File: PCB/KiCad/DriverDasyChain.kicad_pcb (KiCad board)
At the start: 4 copper layers, 70 x 70 mm, 50 parts, among them J1 Conn_01x03, J10 Conn_01x04, J12 Conn_01x04, J2 Conn_01x03, J3 Conn_01x03, J4 Conn_01x04, J5 Conn_01x03, J6 Conn_01x04, Q2 Q_NMOS_GDS, SW1 SW_DIP_x02, SW2 SW_SPDT, U1 AP2112K-3.3, U2 XIAO-ESP32-S3-DIP, U3 74AHCT1G125, U4 SN65HVD230

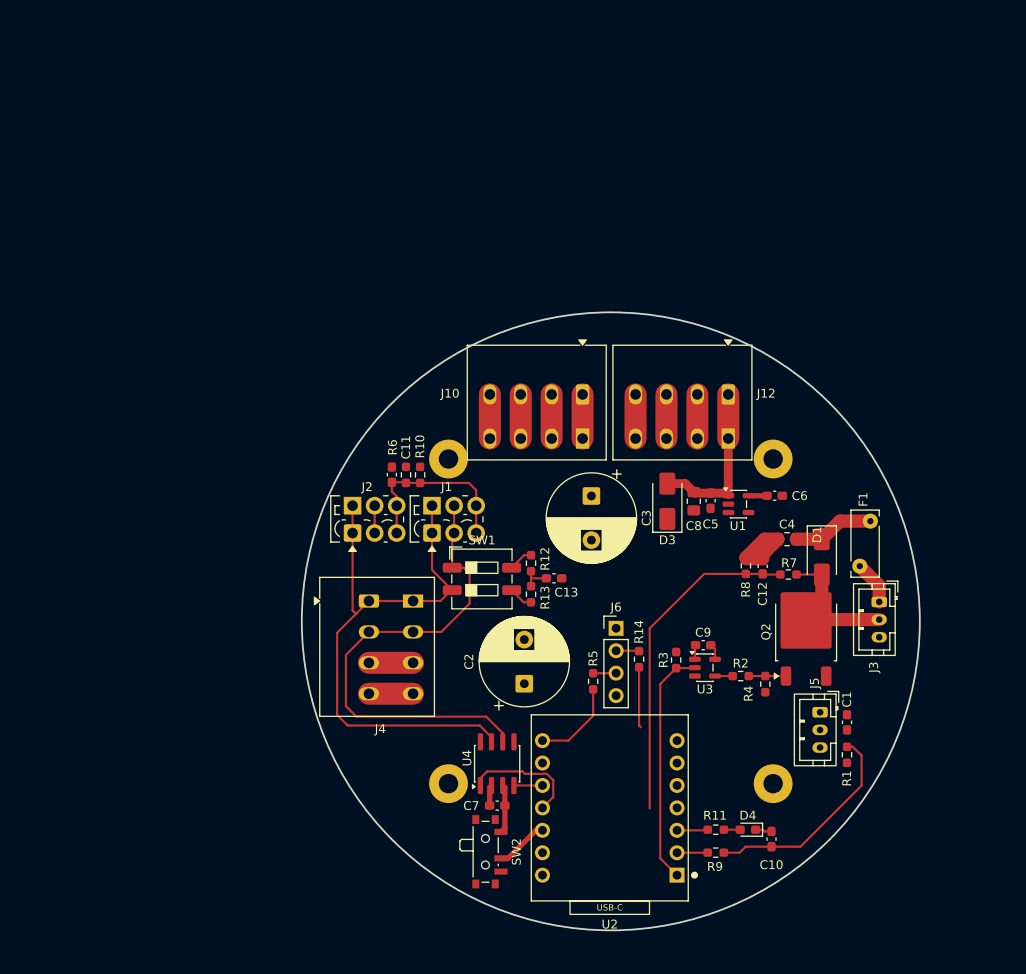
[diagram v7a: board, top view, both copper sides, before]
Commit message: Refactor PCB files and update documentation
- Deleted lock file for the PCB layout.
- Updated lock file for the schematic with new hostname.
- Modified PCB daisy chain documentation to clarify connections and component specifications, including:
  - Revised homing sensor pinout.
  - Added new component for CAN-TVS protection.
  - Adjusted capacitor counts and specifications.
  - Updated notes regarding BOM and assembly instructions.
- Created a new design rule file to enforce solid zone connections for power terminals on specific footprints.
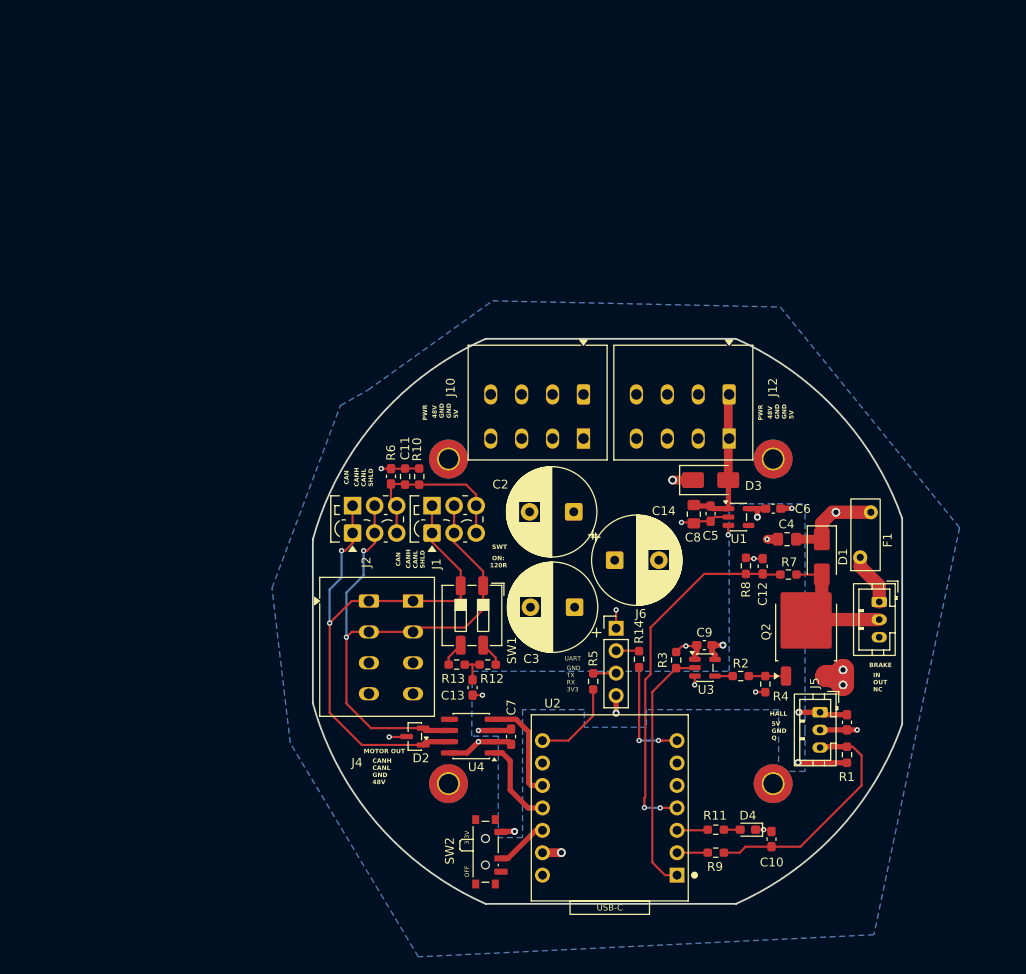
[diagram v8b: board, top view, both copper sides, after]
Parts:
- removed REF** (x4): MountingHole_2.2mm_M2_Pad, MountingHole:MountingHole_2.2mm_M2_Pad
- added C14: 100u, Capacitor_THT:CP_Radial_D10.0mm_P5.00mm, F.Cu at (150.4, 93.1)
- added D2: PESD12VL2BT, Package_TO_SOT_SMD:SOT-23, F.Cu at (127.8, 113.0)
- added H1: MountingHole, MountingHole:MountingHole_2.2mm_M2_Pad_TopBottom, F.Cu at (168.4, 118.4)
- added H2: MountingHole, MountingHole:MountingHole_2.2mm_M2_Pad_TopBottom, F.Cu at (131.6, 118.4)
- added H3: MountingHole, MountingHole:MountingHole_2.2mm_M2_Pad_TopBottom, F.Cu at (168.4, 81.6)
- added H4: MountingHole, MountingHole:MountingHole_2.2mm_M2_Pad_TopBottom, F.Cu at (131.6, 81.6)
- D1: value US2DA -> US1D
- F1: value Polyfuse -> 60R050XU; footprint Fuse:Fuse_Bourns_MF-RHT050 -> R0192:Fuse_Littelfuse_60R050XU
- Q2: value Q_NMOS_GDS -> IRLR3410TRPBF
- moved C2 20.3 mm to (145.8, 87.6), turned to 180 degrees
- moved C13 15.4 mm to (134.3, 107.5), turned to -90 degrees
- moved C3 12.7 mm to (145.9, 98.4), turned to 180 degrees
- moved R12 12.5 mm to (136.1, 104.9), turned to 0 degrees
- moved R13 11.6 mm to (132.5, 104.9), turned to 0 degrees
- moved C7 7.97 mm to (138.7, 113.1), turned to 90 degrees
- moved D3 5.46 mm to (161.3, 84.0), turned to 0 degrees
- moved SW1 4.29 mm to (134.3, 99.3), turned to -90 degrees
- moved U4 4.28 mm to (134.2, 113.0), turned to 180 degrees
- moved C6 1.47 mm to (168.4, 87.2)
- moved U1 1.46 mm to (164.5, 88.2)
- moved C5 1.46 mm to (161.3, 87.8)
- moved C8 1.46 mm to (159.4, 87.9)
- moved F1 1.00 mm to (178.2, 92.8)
- moved C11 0.21 mm to (125.1, 83.6)
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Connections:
- C2 pad 1: GND -> +48V
- C2 pad 2: +48V -> GND
- C3 pad 1: GND -> +48V
- C3 pad 2: +48V -> GND
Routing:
- net +48V: track 24.2 -> 10.8 mm, vias 0 -> 1
- net GND: track 40.2 -> 51.1 mm, vias 0 -> 18
- net /CANL: track 58.1 -> 67.2 mm, vias 0 -> 2
- net /CAN RX: track 3.23 -> 12.1 mm
- net +3.3V: track 7.63 -> 15.8 mm, vias 0 -> 5
- net /GPIO D6 (XIAO-ESP32-S3): track 6.88 -> 12.6 mm, vias 0 -> 2
- net /GPIO D3 (XIAO-ESP32-S3): track 37.8 -> 41.6 mm, vias 0 -> 2
- net /CAN TX: track 13.5 -> 10.1 mm
- net /TLE4905L Out: track 24.2 -> 27.3 mm
- net /GPIO D0 (XIAO-ESP32-S3): track 27.1 -> 28.7 mm
- net /CANH: track 66.3 -> 67.8 mm, vias 0 -> 2
- net +5V: track 25.6 -> 26.8 mm, vias 0 -> 3
- net /BRAKE +48V: track 4.96 -> 5.94 mm
- added copper zone on B.Cu, net +3.3V
- added copper zone on In2.Cu, net +48V
- added copper zone on In2.Cu, net +5V
- added copper zone on B.Cu, net GND
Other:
- board size 70 x 70 mm -> 66.8 x 64 mm
- board text added: "48V GND GND 5V"
- board text added: "5V GND Q"
- board text added: "BRAKE"
- board text added: "CAN"
- board text added: "CANH CANL GND 48V"
- board text added: "CANH CANL SHLD"
- board text added: "GND TX RX 3V3"
- board text added: "HALL"
- board text added: "IN OUT NC"
- board text added: "MOTOR OUT"
- board text added: "OFF 3.3V"
- board text added: "ON: 120R"
- board text added: "PWR"
- board text added: "SWT"
- board text added: "UART"
